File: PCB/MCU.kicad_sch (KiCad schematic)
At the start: 0 parts

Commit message: Diseño MCU ESP32-S3 y USB-C conector
Se diseño el ESP32-S3-WROOM-1 junto a su conector USB-C para flashear el MCU
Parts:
- added C200, C201, C203: 0.1uF, Capacitor_SMD:C_0603_1608Metric_Pad1.08x0.95mm_HandSolder, symbol Device:C_Small
- added C202: 22uF, Capacitor_SMD:C_0603_1608Metric_Pad1.08x0.95mm_HandSolder, symbol Device:C_Small
- added D200, D201, D202: LESD5D5.0CT1G, symbol Device:D_TVS
- added J200: TYPE-C-31-M-12, TYPE-C-31-M-12:TYPE-C-31-M-12, symbol TYPE-C-31-M-12:TYPE-C-31-M-12
- added R200: 10K, Resistor_SMD:R_0603_1608Metric, symbol Device:R_Small
- added R201, R202: 5.1K, Resistor_SMD:R_0603_1608Metric, symbol Device:R_Small
- added S200, S201: TS-1187A-B-A-B, TS-1187A-B-A-B:SW_TS-1187A-B-A-B, symbol TS-1187A-B-A-B:TS-1187A-B-A-B
- added U200: ESP32-S3-WROOM-1, RF_Module:ESP32-S3-WROOM-1, symbol RF_Module:ESP32-S3-WROOM-1
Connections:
- new net: J200.A5 (CC1), R201.1
- new net: J200.B5 (CC2), R202.1
- new net +3.3V: C202.1, C203.1, R200.1, U200.2 (3V3)
- new net BOOT: C201.1, S201.C, S201.D, U200.27 (IO0)
- new net EN: C200.1, R200.2, S200.C, S200.D, U200.3 (EN)
- new net FLT: U200.18 (IO10)
- new net GND: C200.2, C201.2, C202.2, C203.2, D200.1 (A1), D201.1 (A1), D202.1 (A1), J200.A1_B12 (GND), J200.B1_A12 (GND), J200.S1 (SHIELD), J200.S2 (SHIELD), J200.S3 (SHIELD), J200.S4 (SHIELD), R201.2, R202.2, S200.A, S200.B, S201.A, S201.B, U200.1 (GND), U200.40 (GND), U200.41 (GND)
- new net USB_N: D202.2 (A2), J200.A7 (DN1), J200.B7 (DN2), U200.13 (IO19)
- new net USB_P: D201.2 (A2), J200.A6 (DP1), J200.B6 (DP2), U200.14 (IO20)
- new net VBUS: D200.2 (A2), J200.A4_B9 (VBUS), J200.B4_A9 (VBUS)
- no-connect marks 0 -> 2
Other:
- note added: "MCU"
- note added: "USB TYPE-C"
- note added: "[2] MCU"

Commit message: Agregado RS485, Smart Switch, ORING Diode
Se termino de acabar todo el esquematico, solo falta crear el footprint para un inductor
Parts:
- removed D200, D201, D202: LESD5D5.0CT1G, symbol Device:D_TVS
- added C204: 0.1uF, Capacitor_SMD:C_0603_1608Metric_Pad1.08x0.95mm_HandSolder, symbol Device:C_Small
- added D200: PMEG3030EP,115, Diode_SMD:D_SOD-128, symbol Diode:PMEG4050EP
- added J2: 2086-1104, 2086-1104-THT:2086-1104-THT, symbol 2086-1104-THT:2086-1104
- added U201: USBLC6-2SC6, Package_TO_SOT_SMD:SOT-23-6, symbol Power_Protection:USBLC6-2SC6
- S200, S201: footprint TS-1187A-B-A-B:SW_TS-1187A-B-A-B -> TS-1187A-B-A-B:TS-1187A-B-A-B
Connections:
- net GND: now also C204.2, J2.P4_1, J2.P4_2, U201.2 (GND)
- net USB_N: now also J2.P2_1, J2.P2_2, U201.4 (I/O2); no longer J200.B7 (DN2)
- net USB_P: now also J2.P1_1, J2.P1_2, U201.6 (I/O1); no longer J200.B6 (DP2)
- net VBUS: now also C204.1, D200.2 (A), J2.P3_1, J2.P3_2, U201.5 (VBUS)
- net DOOR_EN: now reaches U200.19 (IO11)
- net DOOR_DIAG_EN: now reaches U200.20 (IO12)
- net DOOR_FAULT: now reaches U200.21 (IO13)
- net ID1: now reaches U200.22 (IO14)
- net ID2: now reaches U200.23 (IO21)
- net ID3: now reaches U200.24 (IO47)
- net ID4: now reaches U200.25 (IO48)
- net ID5: now reaches U200.26 (IO45)
- net RX: now reaches U200.36 (RXD0)
- net TX: now reaches U200.37 (TXD0)
- net RS485_EN: now reaches U200.39 (IO1)
- new net: J200.B6 (DP2), U201.1 (I/O1)
- new net: J200.B7 (DN2), U201.3 (I/O2)
- new net 12V_5V: D200.1 (K)
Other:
- note added: "USB TYPE-C CONNECTOR"

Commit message: Placement
Se termino de crear el footprint para el inductor y placement en la PCB
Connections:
- net DOOR_EN: now also U200.21 (IO13); no longer U200.19 (IO11)
- net DOOR_FAULT: now also U200.19 (IO11); no longer U200.21 (IO13)
- net ID3: now also U200.33 (IO40); no longer U200.24 (IO47)
- net ID4: now also U200.34 (IO41); no longer U200.25 (IO48)
- net ID5: now also U200.35 (IO42); no longer U200.26 (IO45)
- net USB_N: no longer J200.A7 (DN1)
- net USB_P: no longer J200.A6 (DP1)
- net N: now reaches U201.1 (I/O1)
- net N: now also J200.A7 (DN1), J200.B7 (DN2); no longer J200.B6 (DP2)
- net P: now reaches U201.3 (I/O2)
- net P: now also J200.A6 (DP1), J200.B6 (DP2); no longer J200.B7 (DN2)
- no-connect marks 2 -> 23
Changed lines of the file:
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@@
+	)
+	(no_connect
+		(at 104.394 114.3)
+	)
+	(no_connect
+		(at 104.394 96.52)
+	)
+	(no_connect
+		(at 104.394 83.82)
+	)
+	(no_connect
+		(at 104.394 86.36)
+	)
+	(no_connect
+		(at 104.394 116.84)
+	)
+	(no_connect
+		(at 134.874 111.76)
+	)
+	(no_connect
+		(at 104.394 99.06)
+	)
+	(no_connect
+		(at 134.874 93.98)
+	)
+	(no_connect
+		(at 104.394 93.98)
+	)
+	(no_connect
+		(at 104.394 91.44)
+	)
+	(no_connect
+		(at 134.874 91.44)
+	)
+	(no_connect
+		(at 134.874 96.52)
+	)
+	(no_connect
+		(at 134.874 116.84)
+	)
+	(no_connect
+		(at 104.394 88.9)
+	)
+	(no_connect
+		(at 104.394 81.28)
 	)
 	(no_connect
 		(at 178.562 72.898)
 	)
-	(wire
-		(pts
-			(xy 214.122 67.818) (xy 218.948 67.818)
+	(no_connect
+		(at 134.874 88.9)
+	)
+	(no_connect
+		(at 134.874 109.22)
+	)
+	(no_connect
+		(at 134.874 99.06)
+	)
+	(no_connect
+		(at 134.874 76.2)
+	)
+	(no_connect
+		(at 134.874 78.74)
+	)
+	(no_connect
+		(at 134.874 114.3)
+	)
+	(wire
+		(pts
+			(xy 214.122 67.818) (xy 238.506 67.818)
 		)
 		(stroke
@@
 	(wire
 		(pts
-			(xy 223.774 67.31) (xy 238.506 67.31)
-		)
-		(stroke
-			(width 0)
-			(type default)
-		)
-	)
-	(wire
-		(pts
 			(xy 119.634 55.88) (xy 119.634 57.15)
 		)
@@
 	(wire
 		(pts
-			(xy 218.948 71.374) (xy 226.06 71.374)
-		)
-		(stroke
-			(width 0)
-			(type default)
-		)
-	)
-	(wire
-		(pts
 			(xy 245.618 60.198) (xy 243.586 60.198)
 		)
@@
 	(wire
 		(pts
-			(xy 226.06 69.85) (xy 238.506 69.85)
-		)
-		(stroke
-			(width 0)
-			(type default)
-		)
-	)
-	(wire
-		(pts
 			(xy 183.388 130.302) (xy 186.436 130.302)
 		)
@@
 	(wire
 		(pts
+			(xy 238.506 67.818) (xy 238.506 67.31)
+		)
+		(stroke
+			(width 0)
+			(type default)
+		)
+	)
+	(wire
+		(pts
+			(xy 134.874 104.14) (xy 137.16 104.14)
+		)
+		(stroke
+			(width 0)
+			(type default)
+		)
+	)
+	(wire
+		(pts
 			(xy 215.646 77.978) (xy 215.646 80.518)
 		)
@@
 	(wire
 		(pts
-			(xy 218.948 67.818) (xy 218.948 71.374)
-		)
-		(stroke
-			(width 0)
-			(type default)
-		)
-	)
-	(wire
-		(pts
 			(xy 178.562 65.278) (xy 168.91 65.278)
 		)
@@
 	(wire
 		(pts
+			(xy 134.874 101.6) (xy 137.16 101.6)
+		)
+		(stroke
+			(width 0)
+			(type default)
+		)
+	)
+	(wire
+		(pts
 			(xy 87.63 75.184) (xy 87.63 76.2)
 		)
@@
 	(wire
 		(pts
-			(xy 223.774 70.358) (xy 223.774 67.31)
-		)
-		(stroke
-			(width 0)
-			(type default)
-		)
-	)
-	(wire
-		(pts
 			(xy 87.63 69.342) (xy 87.63 70.104)
 		)
@@
 	(wire
 		(pts
+			(xy 214.122 70.358) (xy 238.506 70.358)
+		)
+		(stroke
+			(width 0)
+			(type default)
+		)
+	)
+	(wire
+		(pts
 			(xy 104.394 71.12) (xy 102.108 71.12)
 		)
@@
 	(wire
 		(pts
-			(xy 134.874 109.22) (xy 137.16 109.22)
+			(xy 134.874 106.68) (xy 137.16 106.68)
 		)
 		(stroke
@@
 	(wire
 		(pts
-			(xy 134.874 116.84) (xy 137.16 116.84)
+			(xy 238.506 70.358) (xy 238.506 69.85)
 		)
 		(stroke
@@
 	(wire
 		(pts
-			(xy 134.874 114.3) (xy 137.16 114.3)
-		)
-		(stroke
-			(width 0)
-			(type default)
-		)
-	)
-	(wire
-		(pts
 			(xy 183.388 132.842) (xy 186.436 132.842)
 		)
@@
 	(wire
 		(pts
-			(xy 226.06 71.374) (xy 226.06 69.85)
-		)
-		(stroke
-			(width 0)
-			(type default)
-		)
-	)
-	(wire
-		(pts
 			(xy 134.874 81.28) (xy 143.256 81.28)
 		)
@@
 		(pts
 			(xy 102.108 69.342) (xy 87.63 69.342)
-		)
-		(stroke
-			(width 0)
-			(type default)
-		)
-	)
-	(wire
-		(pts
-			(xy 214.122 70.358) (xy 223.774 70.358)
 		)
 		(stroke
@@
 		)
 	)
-	(label "USB_P"
+	(label "P"
 		(at 171.704 67.818 0)
 		(fields_autoplaced yes)
@@
 		)
 	)
+	(label "P"
+		(at 217.424 70.358 0)
+		(fields_autoplaced yes)
+		(effects
+			(font
+				(size 1.27 1.27)
+			)
+			(justify left bottom)
+		)
+	)
 	(label "USB_P"
 		(at 143.256 83.82 180)
@@
 		)
 	)
-	(label "USB_N"
+	(label "N"
 		(at 171.704 70.358 0)
 		(fields_autoplaced yes)
@@
 			)
 			(justify right bottom)
+		)
+	)
+	(label "N"
+		(at 217.424 67.818 0)
+		(fields_autoplaced yes)
+		(effects
+			(font
+				(size 1.27 1.27)
+			)
+			(justify left bottom)
 		)
 	)
@@
 	(hierarchical_label "ID3"
 		(shape input)
-		(at 137.16 114.3 0)
+		(at 137.16 101.6 0)
 		(fields_autoplaced yes)
 		(effects
@@
 	(hierarchical_label "DOOR_FAULT"
 		(shape input)
-		(at 101.854 109.22 180)
+		(at 101.854 104.14 180)
 		(fields_autoplaced yes)
 		(effects
@@
 	(hierarchical_label "ID5"
 		(shape input)
-		(at 137.16 109.22 0)
+		(at 137.16 106.68 0)
 		(fields_autoplaced yes)
 		(effects
@@
 	(hierarchical_label "ID4"
 		(shape input)
-		(at 137.16 116.84 0)
+		(at 137.16 104.14 0)
 		(fields_autoplaced yes)
 		(effects
@@
 	(hierarchical_label "DOOR_EN"
 		(shape output)
-		(at 101.854 104.14 180)
-		(fields_autoplaced yes)
-		(effects
+		(at 101.854 109.22 180)
+		(fields_autoplaced yes)
+		(effects

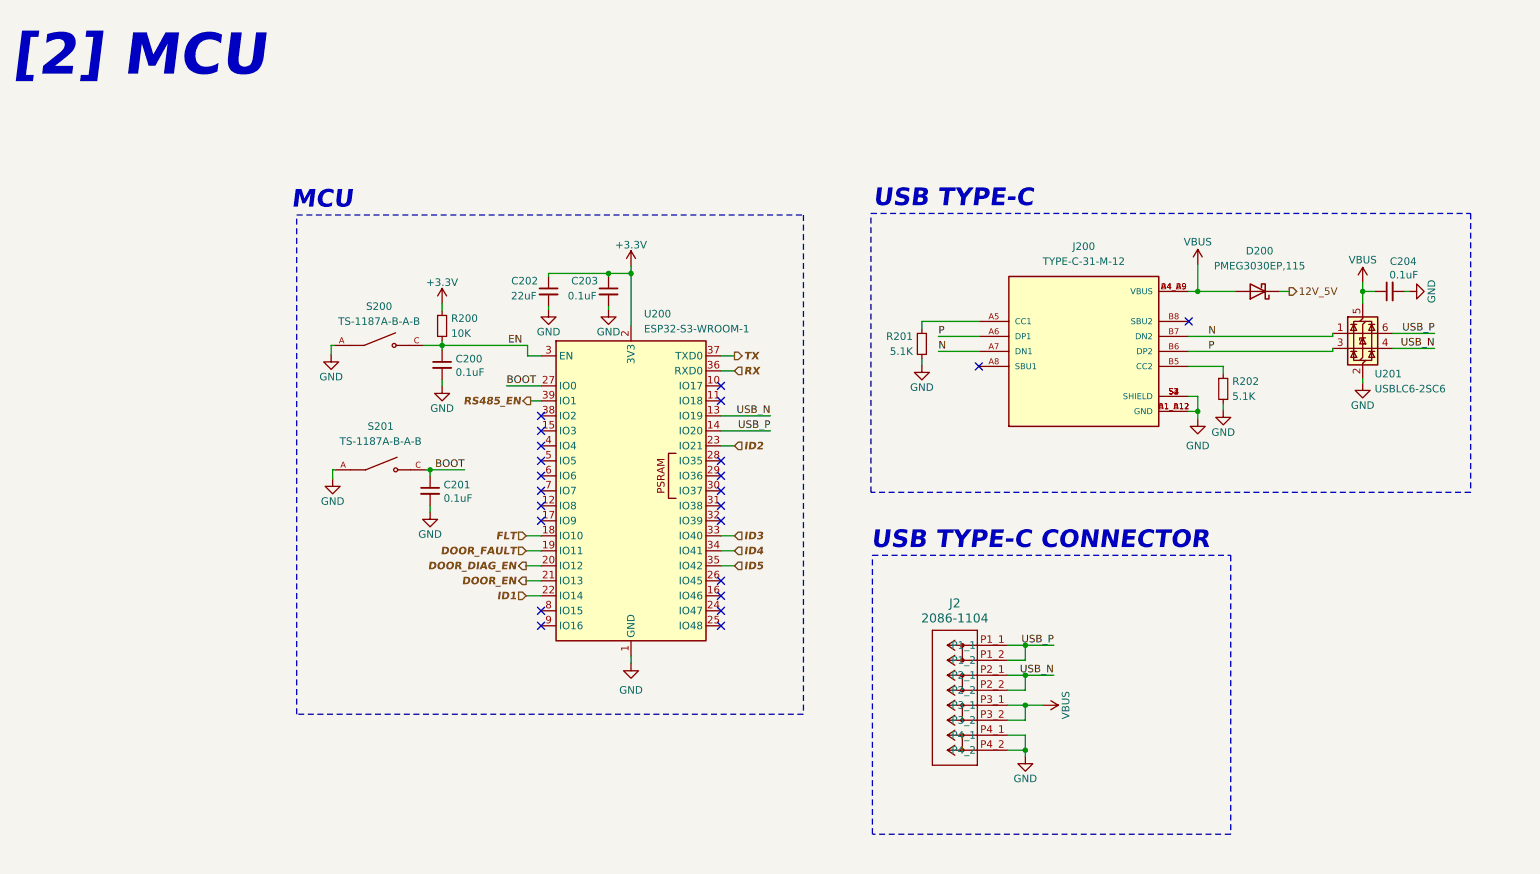
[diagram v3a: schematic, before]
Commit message: PCB acabada con labels
Se agrego:
- Planos de tierra
- Stitching vias
- Labels indicadores para todo los conectores

Se corrigio:
- Errores de librerias de footprint - TPS26631RGE
- Pines sin conectarse
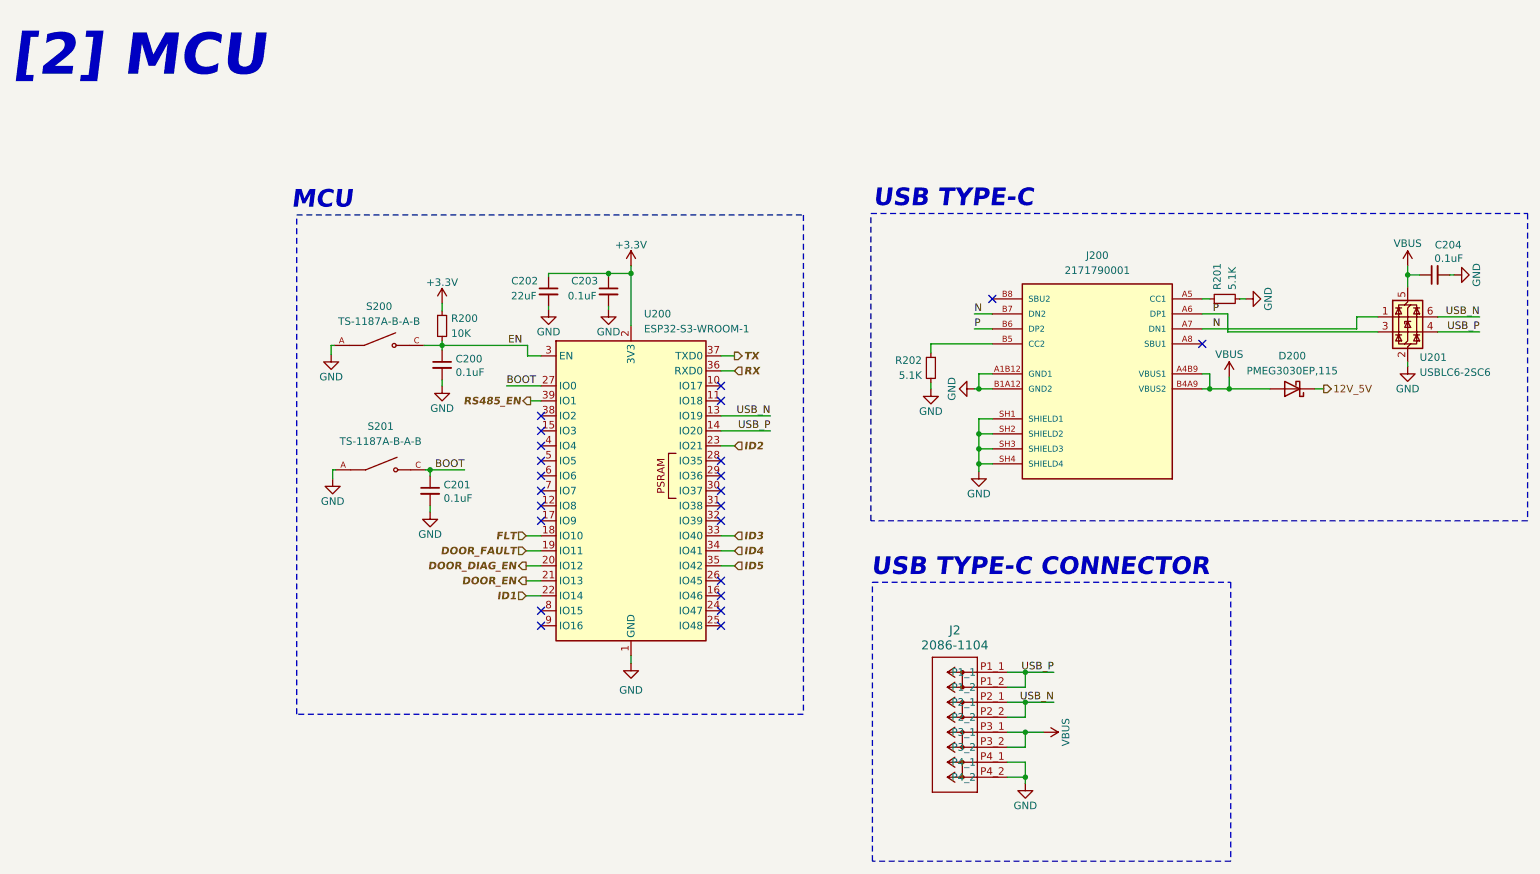
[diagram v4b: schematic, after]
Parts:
- removed J200: TYPE-C-31-M-12, TYPE-C-31-M-12:TYPE-C-31-M-12, symbol TYPE-C-31-M-12:TYPE-C-31-M-12
- added J200: 2171790001, 2171790001:MOLEX_2171790001, symbol 2171790001:2171790001
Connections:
- net GND: now also J200.A1B12 (GND1), J200.B1A12 (GND2), J200.SH1 (SHIELD1), J200.SH2 (SHIELD2), J200.SH3 (SHIELD3), J200.SH4 (SHIELD4)
- net N: now also J200.A7 (DN1), J200.B7 (DN2)
- net P: now also J200.A6 (DP1), J200.B6 (DP2)
- net USB_N: now also U201.6 (I/O1); no longer U201.4 (I/O2)
- net USB_P: now also U201.4 (I/O2); no longer U201.6 (I/O1)
- net VBUS: now also J200.A4B9 (VBUS1), J200.B4A9 (VBUS2)
- net at R201.1: now also J200.A5 (CC1)
- net at R202.1: now also J200.B5 (CC2)
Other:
- moved on the sheet: C204, D200, J2, R201, R202, U201

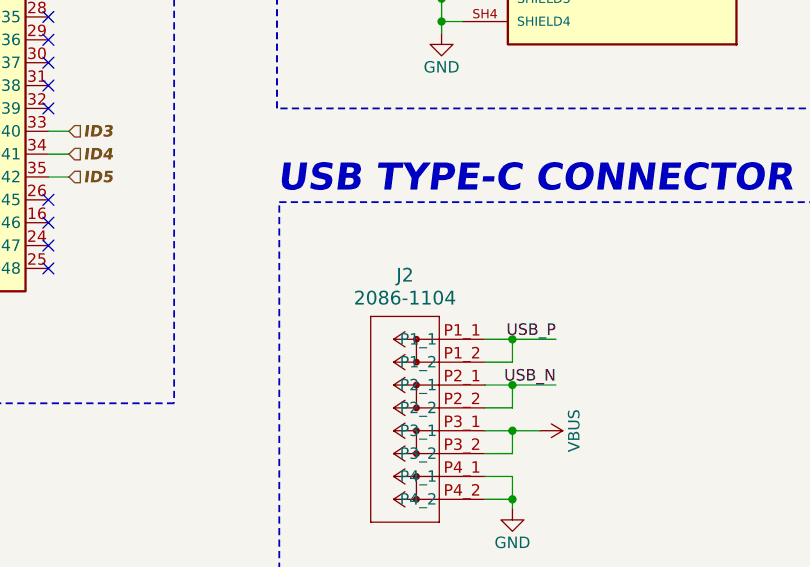
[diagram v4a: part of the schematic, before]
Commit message: Edicion de archivos para JLCPCB
Se ha realizado:
- Cambio de footprint de capacitor 1mF
- Edicion de algunos value references
- Creación de archivos para JLCPCB
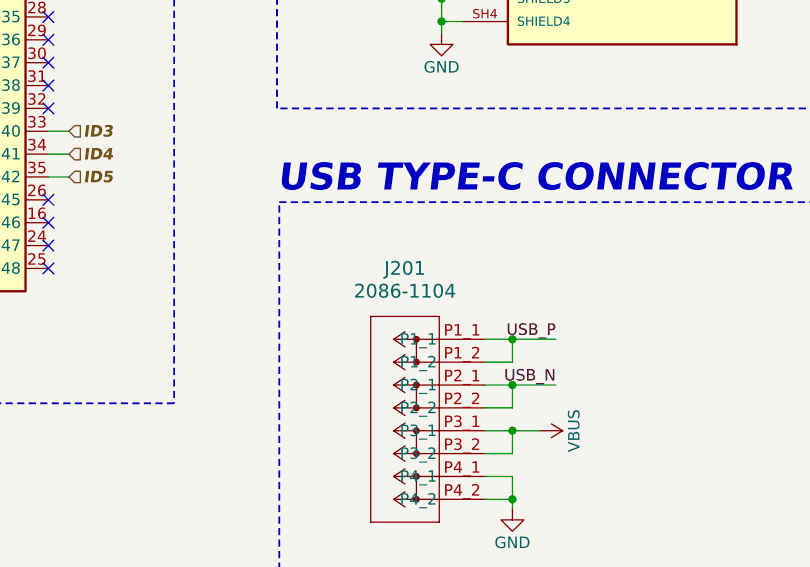
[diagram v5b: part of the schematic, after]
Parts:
- J200: Availability In Stock -> (none); Check_prices https://www.snapeda.com/parts/217179-0001/Molex/view-part/?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 -> (none); Description_1 USB Type C - Connector, Top-mount SMT, 16pos | Molex Incorp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 -> (none); MANUFACTURER Molex -> (none); MAXIMUM_PACKAGE_HEIGHT 3.16 mm -> (none); MF Molex -> (none); MP 217179-0001 -> (none); PARTREV A1 -> (none); Package None -> (none); Price None -> (none); Purchase-URL https://www.snapeda.com/api/url_track_click_mouser/?unipart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 -> (none); STANDARD Manufacturer Recommendations -> (none); SnapEDA_Link https://www.snapeda.com/parts/217179-0001/Molex/view-part/?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 -> (none)
- renumbered J2 to J201
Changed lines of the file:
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@@
-			)
-		)
-		(property "MF" "Molex"
-			(at 198.628 74.168 0)
-			(effects
-				(font
-					(size 1.27 1.27)
-				)
-				(justify bottom)
-				(hide yes)
-			)
-		)
-		(property "MAXIMUM_PACKAGE_HEIGHT" "3.16 mm"
-			(at 198.628 74.168 0)
-			(effects
-				(font
-					(size 1.27 1.27)
-				)
-				(justify bottom)
-				(hide yes)
-			)
-		)
-		(property "Package" "None"
-			(at 198.628 74.168 0)
-			(effects
-				(font
-					(size 1.27 1.27)
-				)
-				(justify bottom)
-				(hide yes)
-			)
-		)
-		(property "Price" "None"
-			(at 198.628 74.168 0)
-			(effects
-				(font
-					(size 1.27 1.27)
-				)
-				(justify bottom)
-				(hide yes)
-			)
-		)
-		(property "Check_prices" "https://www.snapeda.com/parts/217179-0001/Molex/view-part/?ref=eda"
-			(at 198.628 74.168 0)
-			(effects
-				(font
-					(size 1.27 1.27)
-				)
-				(justify bottom)
-				(hide yes)
-			)
-		)
-		(property "STANDARD" "Manufacturer Recommendations"
-			(at 198.628 74.168 0)
-			(effects
-				(font
-					(size 1.27 1.27)
-				)
-				(justify bottom)
-				(hide yes)
-			)
-		)
-		(property "PARTREV" "A1"
-			(at 198.628 74.168 0)
-			(effects
-				(font
-					(size 1.27 1.27)
-				)
-				(justify bottom)
-				(hide yes)
-			)
-		)
-		(property "SnapEDA_Link" "https://www.snapeda.com/parts/217179-0001/Molex/view-part/?ref=snap"
-			(at 198.628 74.168 0)
-			(effects
-				(font
-					(size 1.27 1.27)
-				)
-				(justify bottom)
-				(hide yes)
-			)
-		)
-		(property "MP" "217179-0001"
-			(at 198.628 74.168 0)
-			(effects
-				(font
-					(size 1.27 1.27)
-				)
-				(justify bottom)
-				(hide yes)
-			)
-		)
-		(property "Purchase-URL" "https://www.snapeda.com/api/url_track_click_mouser/?unipart_id=5817784&manufacturer=Molex&part_name=217179-0001&search_term=None"
-			(at 198.628 74.168 0)
-			(effects
-				(font
-					(size 1.27 1.27)
-				)
-				(justify bottom)
-				(hide yes)
-			)
-		)
-		(property "Description_1" "\nUSB Type C - Connector, Top-mount SMT, 16pos | Molex Incorporated 217179-0001\n"
-			(at 198.628 74.168 0)
-			(effects
-				(font
-					(size 1.27 1.27)
-				)
-				(justify bottom)
-				(hide yes)
-			)
-		)
-		(property "Availability" "In Stock"
-			(at 198.628 74.168 0)
-			(effects
-				(font
-					(size 1.27 1.27)
-				)
-				(justify bottom)
-				(hide yes)
-			)
-		)
-		(property "MANUFACTURER" "Molex"
-			(at 198.628 74.168 0)
-			(effects
-				(font
-					(size 1.27 1.27)
-				)
-				(justify bottom)
-				(hide yes)
 			)
 		)
@@
 		(dnp no)
 		(fields_autoplaced yes)
-		(property "Reference" "J2"
-			(at 174.498 117.602 0)
+		(property "Reference" "J201"
+			(at 174.498 116.84 0)
 			(effects
 				(font
@@
 		)
 		(property "Value" "2086-1104"
-			(at 174.498 120.142 0)
+			(at 174.498 119.38 0)
 			(effects
 				(font
@@
 			(project ""
 				(path "/118ffa26-3c65-424a-af71-04338c4de0b0/d482c9b0-d3dc-4677-8cda-69da6efb5749"
-					(reference "J2")
-					(unit 1)
-				)
+					(reference "J201")
+					(unit 1)
+				)
